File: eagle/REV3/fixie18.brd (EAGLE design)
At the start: 50 x 50 mm, 33 parts, among them IC1 74LS595D, J1 CON_HEADER_1X06-PTH, J2 CON_HEADER_1X06-PTH, Q1 MMBT5088

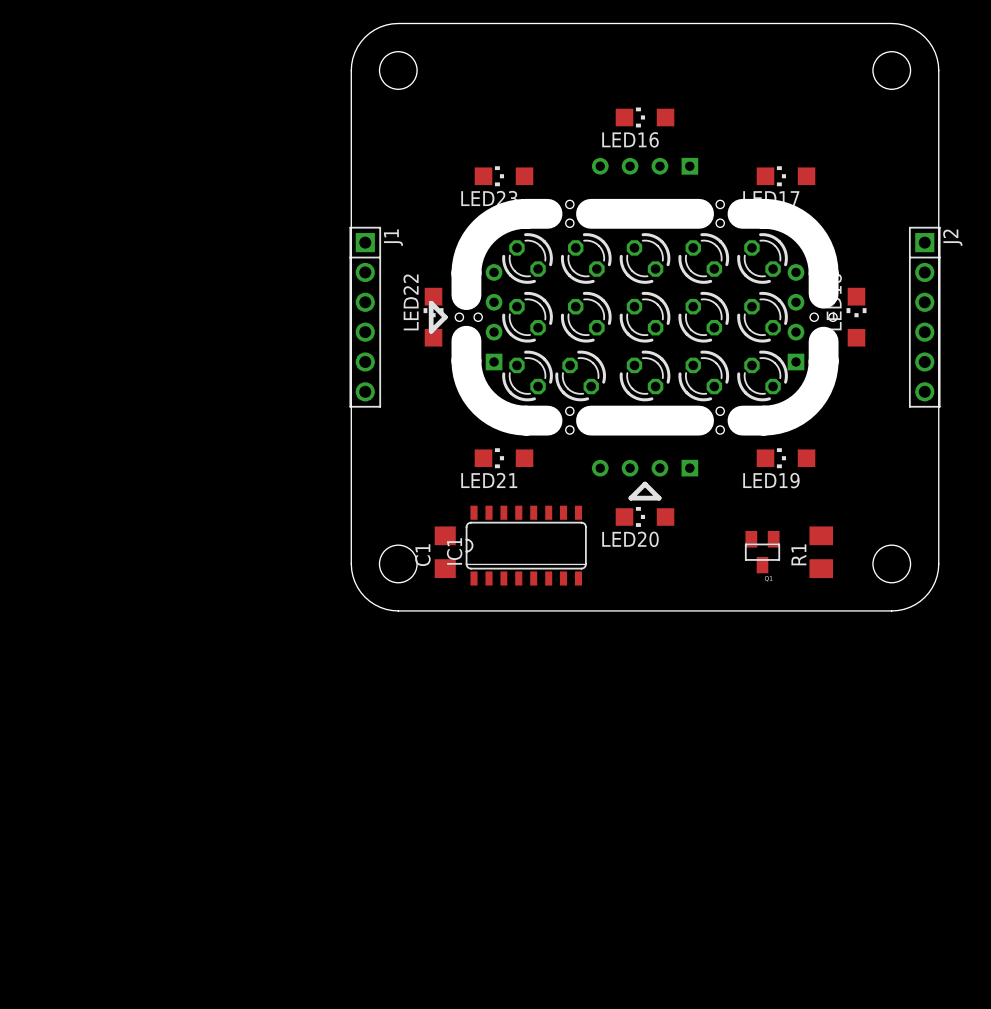
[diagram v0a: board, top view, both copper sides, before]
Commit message: Full Rev3 Version by Alex
Used the unfinished rev3 Version to build a one 5x5cm PCB Version. With
some additional Features: second shift-register for Ring LEDs, optional
ATmega8/328 to control one or multiple PCBs.
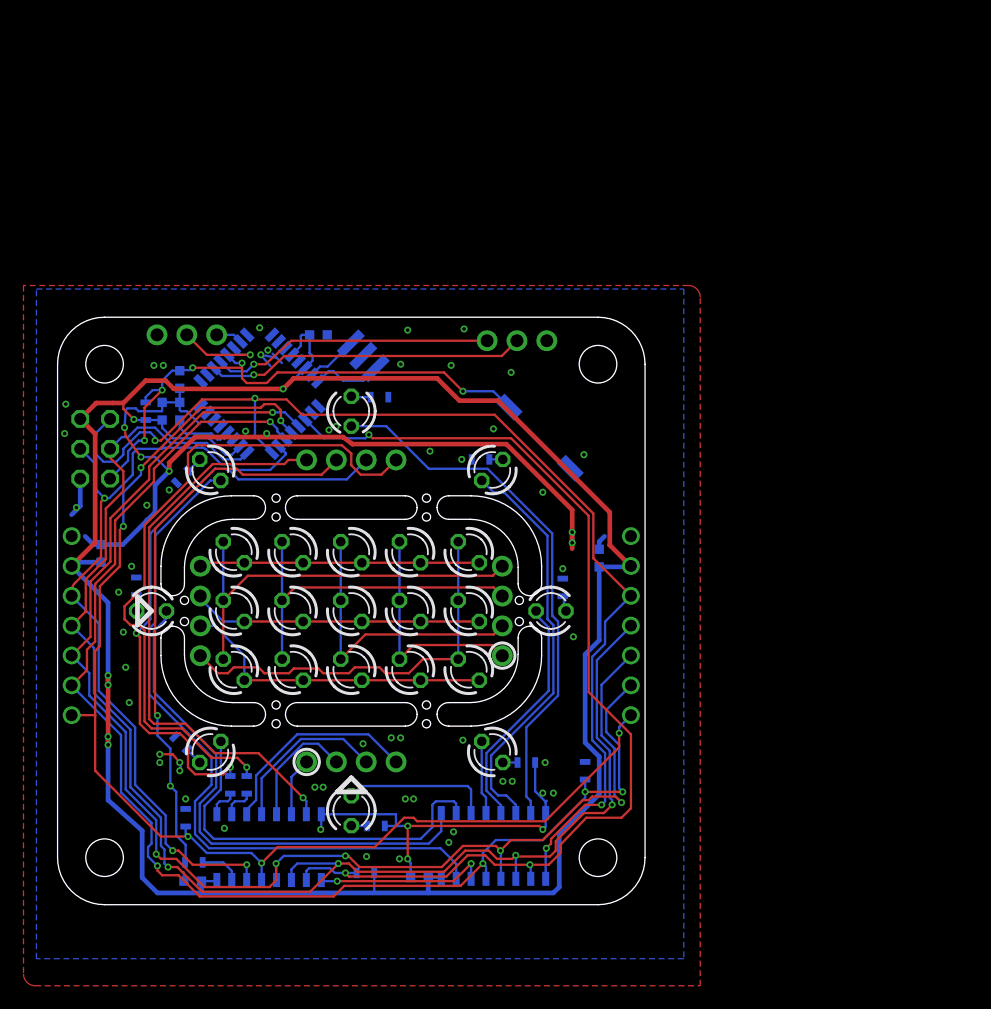
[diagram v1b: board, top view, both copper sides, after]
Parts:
- removed J1, J2: CON_HEADER_1X06-PTH, dp_devices:M1X6
- added C2: 1u, rcl:C0603-VISHAY
- added C3, C4, C5, C6: 0.1, rcl:C0603-VISHAY
- added C7, C8: 100n, rcl:C0603-VISHAY
- added IC2: 74LS595D, SparkFun-DigitalIC:SO16
- added IC3: MEGA8-AI, atmel:TQFP32-08
- added JP5: (no value), pinhead:2X03
- added JP6, JP7: (no value), pinhead:1X03_ROUND_NOSM
- added JP8, JP9: (no value), pinhead:1X04_ROUND_NOSM
- added R10, R11, R12, R13, R14, R15, R5, R6, R7, R8, R9: (no value), rcl:ADAFRUIT_R0603-VISHAY
- added R2, R3: 1k, rcl:ADAFRUIT_R0603-VISHAY
- added R4: 10k, rcl:ADAFRUIT_R0603-VISHAY
- added S1: (no value), _miniRoboter:SMDSWITCH
- added U$1: (no value), dp_pcb:DP5050_V1
- C1: value (none) -> 1u; device rcl:C1206 -> rcl:C0603-VISHAY
- JP1, JP2: value HEADER_CENTERED_04 -> (none); device fixie18:HEADER_04_CENTERED -> pinhead:1X07_RNDNOSILK
- JP3, JP4: value HEADER_CENTERED_04 -> (none); device fixie18:HEADER_04_CENTERED -> pinhead:1X04_ROUND_NOSM
- LED16, LED17, LED18, LED19, LED20, LED21, LED22, LED23: device led:CHIPLED_1206 -> led:LED3MM
- Q1: value MMBT5088 -> CSTCR6M00G53Z; device SparkFun-DiscreteSemi:SOT23 -> murata-filter:CSTCR6M
- R1: value (none) -> 1k; device rcl:M1206 -> rcl:ADAFRUIT_R0603-VISHAY
- moved JP2 67.0 mm to (-23.8, -1.25)
- moved LED6 52.8 mm to (-12.0, -12.0), turned to 225 degrees
- moved LED14 51.5 mm to (-10.0, 0.00)
- moved LED15 50.0 mm to (-5.00, 0.00)
- moved LED9 49.5 mm to (-10.0, -5.00)
- moved LED17 48.9 mm to (5.00, 0.00), turned to 135 degrees
- moved LED16 48.9 mm to (0.00, 0.00), turned to 135 degrees
- moved LED19 47.7 mm to (-10.0, 5.00), turned to 135 degrees
- moved LED5 46.5 mm to (0.00, -17.0), turned to 270 degrees
- moved LED7 46.5 mm to (-17.0, 0.00), turned to 180 degrees
- moved LED12 43.0 mm to (5.00, -5.00)
- moved LED10 43.0 mm to (-4.98, -5.00)
- moved LED11 42.4 mm to (0.00, -5.00)
- moved LED18 41.4 mm to (10.0, 0.00), turned to 135 degrees
- moved LED8 39.2 mm to (-12.0, 12.0)
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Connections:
- removed net N$1: Q1.1, R1.2
- removed net VCC: IC1.16
- new net !CLR: IC1.10, IC2.10, IC3.11, R3.1
- new net +5V: C1.1, C2.1, C3.2, C4.2, C7.1, C8.1, IC1.16, IC2.16, IC3.18, IC3.4, IC3.6, JP1.6, JP2.6, JP5.2, R3.2, R4.2
- new net 1: JP4.3, R6.2
- new net 2: JP4.2, R7.2
- new net 3: JP4.1, R9.2
- new net A: IC1.3, JP3.4
- new net B: IC1.4, JP3.3
- new net C: IC1.5, JP3.2
- new net CLK: IC1.11, IC2.11, IC3.17, JP1.4, JP2.4, JP5.3
- new net COL_1: JP9.3, LED10.A, LED11.A, LED12.A, LED13.A, LED9.A
- new net COL_2: JP9.2, LED14.A, LED15.A, LED16.A, LED17.A, LED18.A
- new net COL_3: JP9.1, LED19.A, LED20.A, LED21.A, LED22.A, LED23.A
- new net D: IC1.6, JP3.1
- new net E: IC1.7, JP4.4
- new net LATCH: IC1.12, IC2.12, IC3.12, JP1.3, JP2.3
- new net MATRIX_EN: IC1.13, IC3.13, JP1.1, JP2.1, R2.2
- new net MCU_RST: C6.2, IC3.29, JP5.5, R4.1, S1.P$2
- new net N$10: IC1.15, R6.1
- new net N$11: IC1.1, R7.1
- new net N$12: IC1.2, R9.1
- new net N$13: LED1.K, R5.2
- new net N$14: LED2.K, R8.2
- new net N$15: LED3.K, R10.2
- new net N$16: LED4.K, R11.2
- new net N$17: LED5.K, R12.2
- new net N$18: LED6.K, R13.2
- new net N$19: LED7.K, R14.2
- new net N$2: IC2.7, LED1.A
- new net N$20: LED8.K, R15.2
- new net N$21: IC1.9, IC2.14
- new net N$24: IC3.32
- new net N$25: IC3.1
- new net N$26: IC3.2
- new net N$27: IC3.9
- new net N$28: IC3.10
- new net N$3: IC2.6, LED2.A
- new net N$30: IC3.23
- new net N$31: IC3.24
- new net N$32: IC3.25
- new net N$33: IC3.26
- new net N$36: C5.2, IC3.20
- new net N$38: IC3.19
- new net N$39: IC3.22
- new net N$4: IC2.5, LED3.A
- new net N$5: IC2.4, LED4.A
- new net N$6: IC2.3, LED5.A
- new net N$7: IC2.2, LED6.A
- new net N$8: IC2.1, LED7.A
- new net N$9: IC2.15, LED8.A
- new net PB6: IC3.7, Q1.1
- new net PB7: IC3.8, Q1.3
- new net RING_EN: IC2.13, IC3.14, JP1.2, JP2.2, R1.2
- new net ROW_A: JP8.4, LED14.K, LED19.K, LED9.K
- new net ROW_B: JP8.3, LED10.K, LED15.K, LED20.K
- new net ROW_C: JP8.2, LED11.K, LED16.K, LED21.K
- new net ROW_D: JP8.1, LED12.K, LED17.K, LED22.K
- new net ROW_E: JP9.4, LED13.K, LED18.K, LED23.K
- new net RX: IC3.30, JP7.2
- new net SCL: IC3.28, JP6.3
- new net SDA: IC3.27, JP6.2
- new net SI: IC1.14, IC3.15, JP2.5, JP5.4
- new net SO: IC2.9, IC3.16, JP1.5, JP5.1
- new net TX: IC3.31, JP7.3
- net GND: now also C1.2, C2.2, C3.1, C4.1, C5.1, C6.1, C7.2, C8.2, IC2.8, IC3.21, IC3.3, IC3.5, JP1.7, JP2.7, JP5.6, JP6.1, JP7.1, Q1.2, R1.1, R10.1, R11.1, R12.1, R13.1, R14.1, R15.1, R2.1, R5.1, R8.1, S1.P$1
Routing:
- net +5V: track 0.00 -> 201.2 mm, vias 0 -> 6
- net CLK: track 0.00 -> 122.6 mm, vias 0 -> 4
- net LATCH: track 0.00 -> 118.1 mm, vias 0 -> 6
- net GND: track 0.00 -> 115.9 mm, vias 0 -> 63
- net RING_EN: track 0.00 -> 112.0 mm, vias 0 -> 5
- net MATRIX_EN: track 0.00 -> 103.8 mm, vias 0 -> 6
- net SO: track 0.00 -> 95.9 mm, vias 0 -> 4
- net !CLR: track 0.00 -> 88.7 mm, vias 0 -> 3
- net SI: track 0.00 -> 68.3 mm, vias 0 -> 3
- net N$9: track 0.00 -> 60.5 mm
- net 3: track 0.00 -> 57.4 mm, vias 0 -> 1
- net 2: track 0.00 -> 50.3 mm, vias 0 -> 2
- net E: track 0.00 -> 49.5 mm, vias 0 -> 1
- net 1: track 0.00 -> 47.8 mm, vias 0 -> 2
- net MCU_RST: track 0.00 -> 47.5 mm, vias 0 -> 5
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- added copper zone on layer 1, net GND
- added copper zone on layer 16, net GND
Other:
- outline, holes or cut-outs redrawn
- board text added: "@tinyledmatrix"
- board text added: "Alex 01-'18"
- board text added: "GND"
- board text added: "RX"
- board text added: "SCL"
- board text added: "SDA"
- board text added: "TX"
- board text added: "fixieTubes"
- board text added: "reset"
- board text added: "rev0"
